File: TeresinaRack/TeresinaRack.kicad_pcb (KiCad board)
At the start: 12 copper layers, 68 x 40 mm, 204 parts, among them J3 USB_Micro-B, J4 SWD, J5 PATCH_SM_EDGE, Q1 MMBT3904, Q2 MMBT3904, SW1 RESET, SW2 BOOT, U1 STM32H750IBK6, U12 TL074, U13 MCP6004, U14 MCP6004, U15 MCP6004, U16 LM4040DBZ-10, U2 IS25LP064A, U3 AS4C16M32MSA-6BIN, U4 PCM3060, U6 TPS62170DSGR, U7 LD1117S50, U8 USBLC6-2SC6, Y1 16MHz

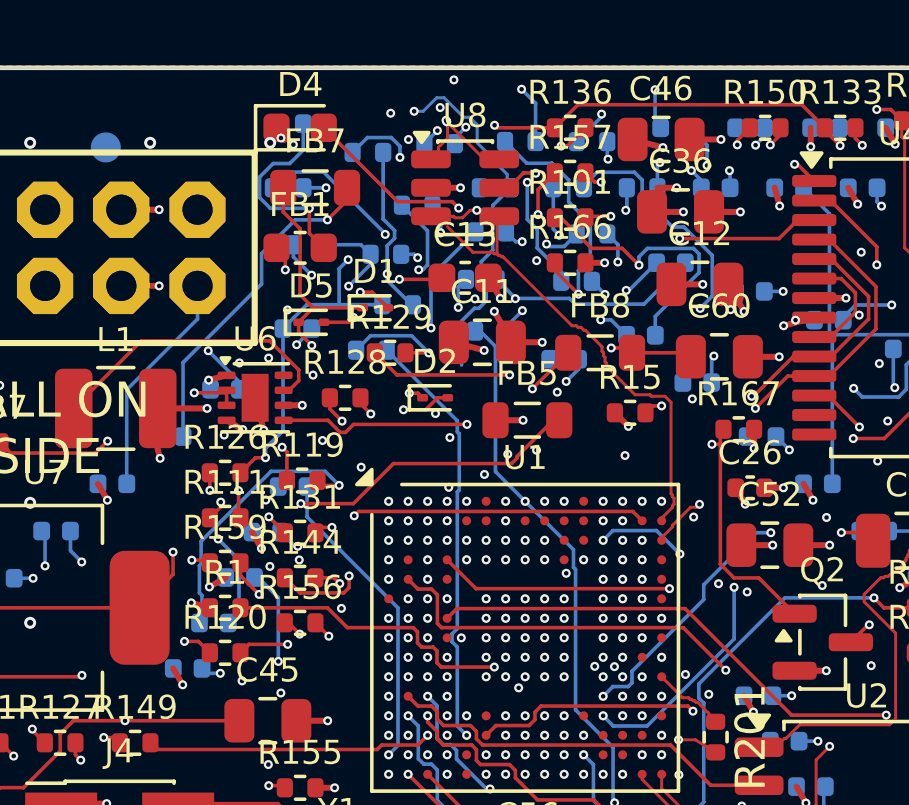
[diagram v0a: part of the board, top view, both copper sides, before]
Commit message: Match official Rev3: audio MFB cap placement + gate-in collector pull-up
Evidence-based re-audit against the official Patch SM Rev3 confirmed the board
is a faithful copy (symbols all match datasheets, analog blocks part-for-part).
Corrected two deviations toward the official design:

- Audio output MFB filter: moved the 18 pF feedback cap (C120/C123) from across
  the 39K T-branch to the op-amp inverting input -- the canonical MFB placement,
  restoring codec-to-single-ended CMRR and phase margin. Schematic relabelled and
  the two nets rerouted on the audio layers; 0 unconnected, DRC unchanged.
- Gate-in collector pull-up 100K -> 10K (R168/R169, LCSC C72443) to match official
  and stay robust if firmware enables an internal pull-down on PG13/PG14.

Also merged a duplicate USB_FS_DM via (cleared the lone hole_to_hole DFM flag) and
fixed a README claim (120K/62K is the official CV-out value, not a 51.5K substitution).
Remaining gate-in base-pulldown (100K vs 1M) / omitted series-R and the gate-out
comparator topology are documented, benign deviations. Regenerated 12-layer fab.
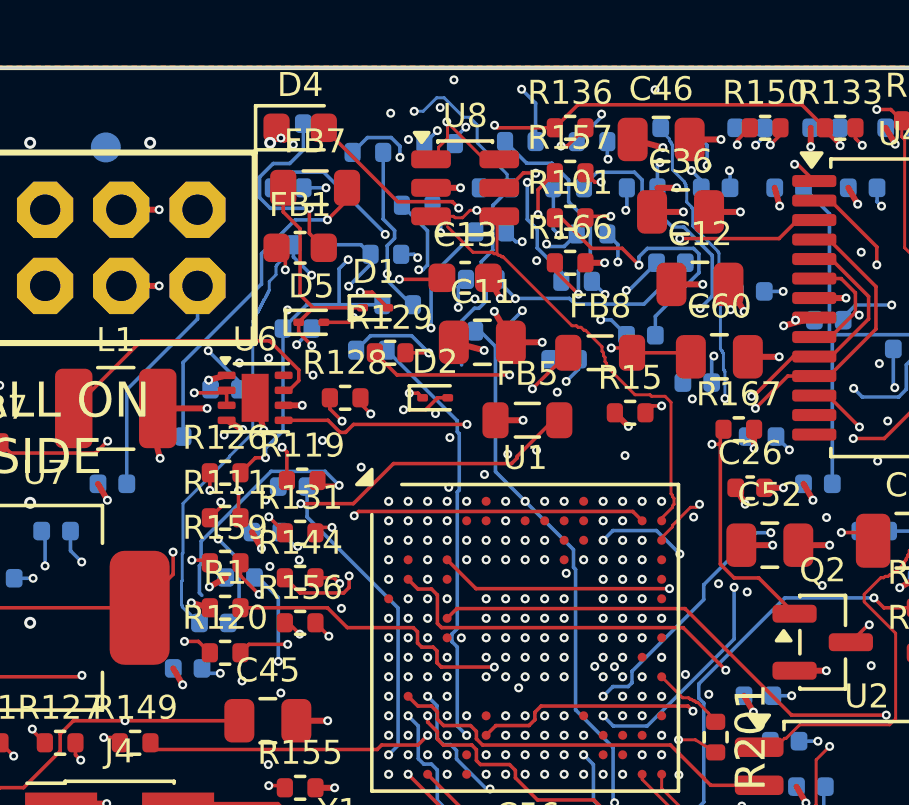
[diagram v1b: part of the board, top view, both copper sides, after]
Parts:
- R168, R169: value 100K -> 10K
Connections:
- C120 pad 2: N_OLA -> OL_INV
- C123 pad 2: N_ORA -> OR_INV
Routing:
- net OR_INV: track 45.8 -> 59.9 mm
- net OL_INV: track 54.9 -> 64.9 mm, vias 3 -> 4
- net N_OLA: track 86.9 -> 85.5 mm
- net N_ORA: track 41.5 -> 40.6 mm
- net USB_FS_DM: track 47.4 -> 47.3 mm, vias 4 -> 3

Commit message: Gate-in base pull-down 100K->1M (R166/R167, LCSC C26083)
Completes the gate-in value match to the official Rev3: base pull-down set to
the official 1M (verified UNI-ROYAL 0402WGF1004TCE = LCSC C26083, in stock at
JLCPCB). Schematic value+LCSC and PCB value updated. Metadata-only (no copper
change); DRC/ERC unchanged.
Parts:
- R166, R167: value 100K -> 1M
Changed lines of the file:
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@@
 			)
 		)
-		(property "Value" "100K"
+		(property "Value" "1M"
 			(at 0 1.17 0)
 			(layer "F.Fab")
@@
 			)
 		)
-		(property "Value" "100K"
+		(property "Value" "1M"
 			(at 0 1.17 0)
 			(layer "F.Fab")
